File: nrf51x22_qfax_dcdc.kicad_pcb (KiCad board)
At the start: 2 copper layers, 17.2 x 15 mm, 57 parts, among them U1 nrf51822-qfax, X1 Crystal-4, X2 32.768kHz

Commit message: add missing x1
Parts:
- removed the REF** at (87.2, -91.4) (x2)
- added REF** (x2): VIA-0.6096, dcdc:VIA-0.6096, F.Cu at (87.2, -91.4)
- X1: footprint BT-XTAL_2016 -> dcdc:BT-XTAL_2016
- turned X1 to 270 degrees
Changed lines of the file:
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@@
 (kicad_pcb (version 4) (host pcbnew 4.0.0-stable)
   (general
-    (links 89)
-    (no_connects 20)
-    (area 71.518807 -97.97362 97.2013 -77.09662)
+    (links 93)
+    (no_connects 19)
+    (area 75.368339 -95.067421 92.766941 -79.878219)
     (thickness 1.6)
     (drawings 26)
@@
     (add_net "Net-(L2-Pad2)")
   )
-  (module BT-XTAL_2016 (layer F.Cu)
-    (at 89.871735 -90.089017)
-    (attr smd)
-    (fp_text reference X1 (at 0 0) (layer F.SilkS) hide
-      (effects (font (thickness 0.05)))
-    )
-    (fp_text value Crystal-4 (at 0 0) (layer F.SilkS) hide
-      (effects (font (thickness 0.05)))
-    )
-  )
   (module dcdc:CAPC1608X06L (layer F.Cu)
     (at 81.744454 -93.396097 40)
@@
       (scale (xyz 1 1 1))
       (rotate (xyz 0 0 360))
+    )
+  )
+  (module dcdc:BT-XTAL_2016 (layer F.Cu)
+    (at 89.871735 -90.089017 270)
+    (attr smd)
+    (fp_text reference X1 (at 0 -3 270) (layer F.SilkS) hide
+      (effects (font (thickness 0.05)))
+    )
+    (fp_text value Crystal-4 (at 0 3 270) (layer F.SilkS) hide
+      (effects (font (thickness 0.05)))
+    )
+    (fp_line (start -1.2 -1.4) (end 1.2 -1.4) (layer F.CrtYd) (width 0.05))
+    (fp_line (start 1.2 -1.4) (end 1.2 1.4) (layer F.CrtYd) (width 0.05))
+    (fp_line (start 1.2 1.4) (end -1.2 1.4) (layer F.CrtYd) (width 0.05))
+    (fp_line (start -1.2 1.4) (end -1.2 -1.4) (layer F.CrtYd) (width 0.05))
+    (fp_line (start 1.05 -0.6) (end 1.05 0.6) (layer F.SilkS) (width 0.15))
+    (fp_line (start -1.05 0.6) (end -1.05 -1) (layer F.SilkS) (width 0.15))
+    (pad 2 smd rect (at -0.55 0.7 180) (size 0.9 0.8) (layers F.Cu F.Paste F.Mask)
+      (net 1 GND))
+    (pad 3 smd rect (at 0.55 0.7 180) (size 0.9 0.8) (layers F.Cu F.Paste F.Mask)
+      (net 3 "Net-(C2-Pad1)"))
+    (pad 1 smd rect (at -0.55 -0.7 180) (size 0.9 0.8) (layers F.Cu F.Paste F.Mask)
+      (net 2 "Net-(C1-Pad1)"))
+    (pad 4 smd rect (at 0.55 -0.7 180) (size 0.9 0.8) (layers F.Cu F.Paste F.Mask)
+      (net 1 GND))
+    (model "${KIPRJMOD}/dcdc.3dshapes/wrl/User Library-GeyerElectronics_KX6.wrl"
+      (at (xyz -0.00028 -0.00028 0))
+      (scale (xyz 0.393701 0.393701 0.393701))
+      (rotate (xyz 270 360 90))
+    )
+    (model ${KIPRJMOD}/dcdc.3dshapes/wrlshp/AFAD9782-D084.wrl
+      (at (xyz 0 0 0))
+      (scale (xyz 1 1 1))
+      (rotate (xyz 0 0 180))
+    )
+    (model ${KIPRJMOD}/dcdc.3dshapes/wrlshp/A6760B87-8591.wrl
+      (at (xyz 0 0 0))
+      (scale (xyz 1 1 1))
+      (rotate (xyz 0 0 0))
     )
   )
@@
   (segment (start 80.39882 -81.90893) (end 80.39882 -85.30782) (width 0.381) (layer B.Cu) (net 1))
   (segment (start 82.70593 -89.10221) (end 82.89304 -89.28931) (width 0.2286) (layer F.Cu) (net 1))
+  (segment (start 90.42253 -90.58902) (end 91.64974 -90.58902) (width 0.1524) (layer F.Cu) (net 2) (status 20))
+  (segment (start 89.87174 -88.92062) (end 89.87174 -90.03822) (width 0.254) (layer F.Cu) (net 2))
+  (segment (start 89.87174 -90.03822) (end 90.42253 -90.58902) (width 0.1524) (layer F.Cu) (net 2))
+  (segment (start 89.69394 -88.74282) (end 89.87174 -88.92062) (width 0.1524) (layer F.Cu) (net 2))
+  (segment (start 88.63771 -88.74282) (end 89.69394 -88.74282) (width 0.1524) (layer F.Cu) (net 2))
   (segment (start 87.98934 -87.42602) (end 87.98934 -88.09445) (width 0.1524) (layer F.Cu) (net 2))
   (segment (start 87.45494 -86.89162) (end 87.98934 -87.42602) (width 0.1524) (layer F.Cu) (net 2) (status 10))
   (segment (start 87.13094 -86.89162) (end 87.45494 -86.89162) (width 0.1524) (layer F.Cu) (net 2) (status 30))
-  (segment (start 90.42253 -90.58902) (end 91.64974 -90.58902) (width 0.1524) (layer F.Cu) (net 2) (status 20))
-  (segment (start 89.87174 -88.92062) (end 89.87174 -90.03822) (width 0.1524) (layer F.Cu) (net 2))
-  (segment (start 89.87174 -90.03822) (end 90.42253 -90.58902) (width 0.1524) (layer F.Cu) (net 2))
   (segment (start 87.98934 -88.09445) (end 88.63771 -88.74282) (width 0.1524) (layer F.Cu) (net 2))
-  (segment (start 88.63771 -88.74282) (end 89.69394 -88.74282) (width 0.1524) (layer F.Cu) (net 2))
-  (segment (start 89.69394 -88.74282) (end 89.87174 -88.92062) (width 0.1524) (layer F.Cu) (net 2))
+  (segment (start 88.99953 -89.58902) (end 89.19953 -89.38902) (width 0.1524) (layer F.Cu) (net 3))
+  (segment (start 88.91786 -89.45402) (end 89.13453 -89.45402) (width 0.1524) (layer F.Cu) (net 3))
+  (segment (start 87.68454 -88.2207) (end 88.91786 -89.45402) (width 0.1524) (layer F.Cu) (net 3))
+  (segment (start 87.68454 -87.55551) (end 87.68454 -88.2207) (width 0.1524) (layer F.Cu) (net 3))
   (segment (start 88.04294 -89.58902) (end 88.99953 -89.58902) (width 0.1524) (layer F.Cu) (net 3) (status 10))
-  (segment (start 88.99953 -89.58902) (end 89.19953 -89.38902) (width 0.1524) (layer F.Cu) (net 3))
   (segment (start 87.42064 -87.29162) (end 87.68454 -87.55551) (width 0.1524) (layer F.Cu) (net 3) (status 10))
   (segment (start 87.13094 -87.29162) (end 87.42064 -87.29162) (width 0.1524) (layer F.Cu) (net 3) (status 30))
-  (segment (start 88.91786 -89.45402) (end 89.13453 -89.45402) (width 0.1524) (layer F.Cu) (net 3))
-  (segment (start 87.68454 -87.55551) (end 87.68454 -88.2207) (width 0.1524) (layer F.Cu) (net 3))
-  (segment (start 87.68454 -88.2207) (end 88.91786 -89.45402) (width 0.1524) (layer F.Cu) (net 3))
   (segment (start 88.29693 -84.98682) (end 89.19393 -84.98682) (width 0.508) (layer F.Cu) (net 4) (status 30))
   (segment (start 87.91571 -84.98183) (end 88.30494 -84.98183) (width 0.2286) (layer F.Cu) (net 4) (status 20))

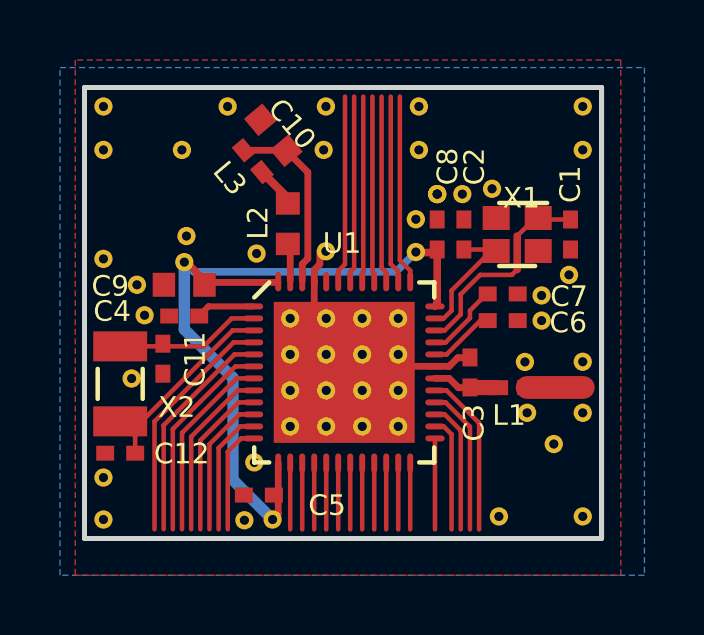
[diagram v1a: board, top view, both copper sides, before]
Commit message: swap 3 via back to vdd, and rotate parts so nets are correct
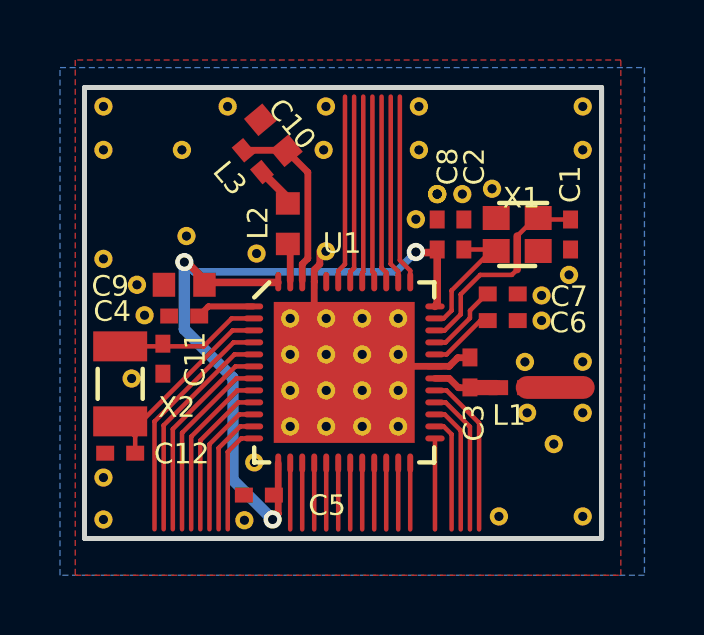
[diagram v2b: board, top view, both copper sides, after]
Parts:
- removed the REF** at (87.2, -91.4) (x2)
- removed the REF** at (78.8, -89.2)
- removed the REF** at (86.5, -89.5)
- removed the REF** at (81.7, -80.6)
- added REF** (x2): VIA-0.6096, dcdc:VIA-0.6096, F.Cu at (87.2, -91.4)
- turned C10 to 220 degrees
- turned C11 to 90 degrees
- turned C12 to 0 degrees
- turned C4 to 0 degrees
- turned C6 to 180 degrees
- turned C7 to 180 degrees
- turned C8 to 270 degrees
- turned C9 to 270 degrees
- turned L2 to 270 degrees
- turned L3 to 40 degrees
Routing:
- net GND: track 38.4 -> 5.62 mm
- net /VDD_nRF: track 1.83 -> 26.1 mm, vias 0 -> 3
- net Net-(C10-Pad2): track 1.77 -> 6.11 mm
- net Net-(C7-Pad2): track 0.36 -> 2.44 mm
- net Net-(C6-Pad2): track 0.39 -> 2.24 mm
- net Net-(L2-Pad1): track 2.56 -> 1.40 mm
- net Net-(L2-Pad2): track 0.18 -> 1.15 mm

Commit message: add grid origin and regen gerbers
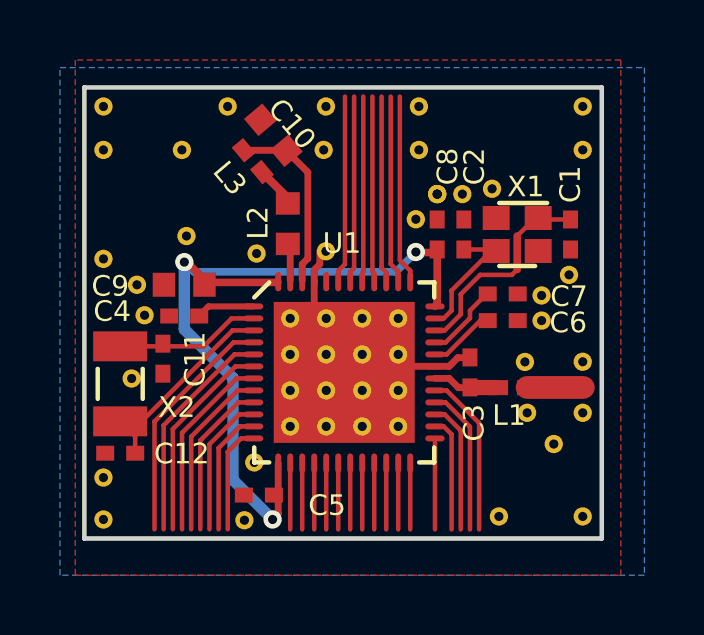
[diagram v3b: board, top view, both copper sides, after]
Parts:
- removed the REF** at (87.2, -91.4) (x2)
- added REF** (x2): VIA-0.6096, dcdc:VIA-0.6096, F.Cu at (87.2, -91.4)
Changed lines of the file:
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@@
     (links 90)
     (no_connects 3)
-    (area 75.368339 -95.067421 92.766941 -79.878219)
+    (area 71.518807 -97.97362 97.2013 -77.09662)
     (thickness 1.6)
-    (drawings 26)
+    (drawings 22)
     (tracks 215)
     (zones 0)
@@
     (pad_drill 0.3048)
     (pad_to_mask_clearance 0)
-    (aux_axis_origin 0 0)
+    (aux_axis_origin 75.44454 -79.95442)
+    (grid_origin 75.44454 -79.95442)
     (visible_elements 7FFFF77F)
     (pcbplotparams
@@
       (viasonmask false)
       (mode 1)
-      (useauxorigin false)
+      (useauxorigin true)
       (hpglpennumber 1)
       (hpglpenspeed 20)
@@
   (gr_line (start 75.44454 -79.95442) (end 75.44454 -94.99122) (layer Edge.Cuts) (width 0.1524))
   (gr_line (start 75.44454 -79.95442) (end 92.69074 -79.95442) (layer Edge.Cuts) (width 0.1524))
-  (gr_line (start 92.69074 -79.95442) (end 92.69074 -94.99122) (layer Edge.Cuts) (width 0.1524))
   (gr_line (start 75.44454 -94.99122) (end 92.69074 -94.99122) (layer Edge.Cuts) (width 0.1524))
-  (gr_line (start 75.44454 -94.99122) (end 92.69074 -94.99122) (layer Edge.Cuts) (width 0.1524))
-  (gr_line (start 75.44454 -79.95442) (end 75.44454 -94.99122) (layer Edge.Cuts) (width 0.1524))
-  (gr_line (start 75.44454 -79.95442) (end 92.69074 -79.95442) (layer Edge.Cuts) (width 0.1524))
   (gr_line (start 92.69074 -79.95442) (end 92.69074 -94.99122) (layer Edge.Cuts) (width 0.1524))
   (gr_text C10 (at 81.76914 -94.48322 310) (layer F.SilkS)
@@
     (effects (font (size 0.6858 0.6858) (thickness 0.1)) (justify left))
   )
-  (gr_text X1 (at 89.38914 -91.30822) (layer F.SilkS)
+  (gr_text X1 (at 89.535 -91.6813) (layer F.SilkS)
     (effects (font (size 0.6858 0.6858) (thickness 0.1)) (justify left))
   )
